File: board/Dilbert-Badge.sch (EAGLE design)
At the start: 28 parts, among them IC1 MCP23017SO, J5 I2C, J6 UART, J7 NEOPIXEL, SW1 UP, SW2 DOWN, SW3 LEFT, SW4 RIGHT, SW5 A, SW6 B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

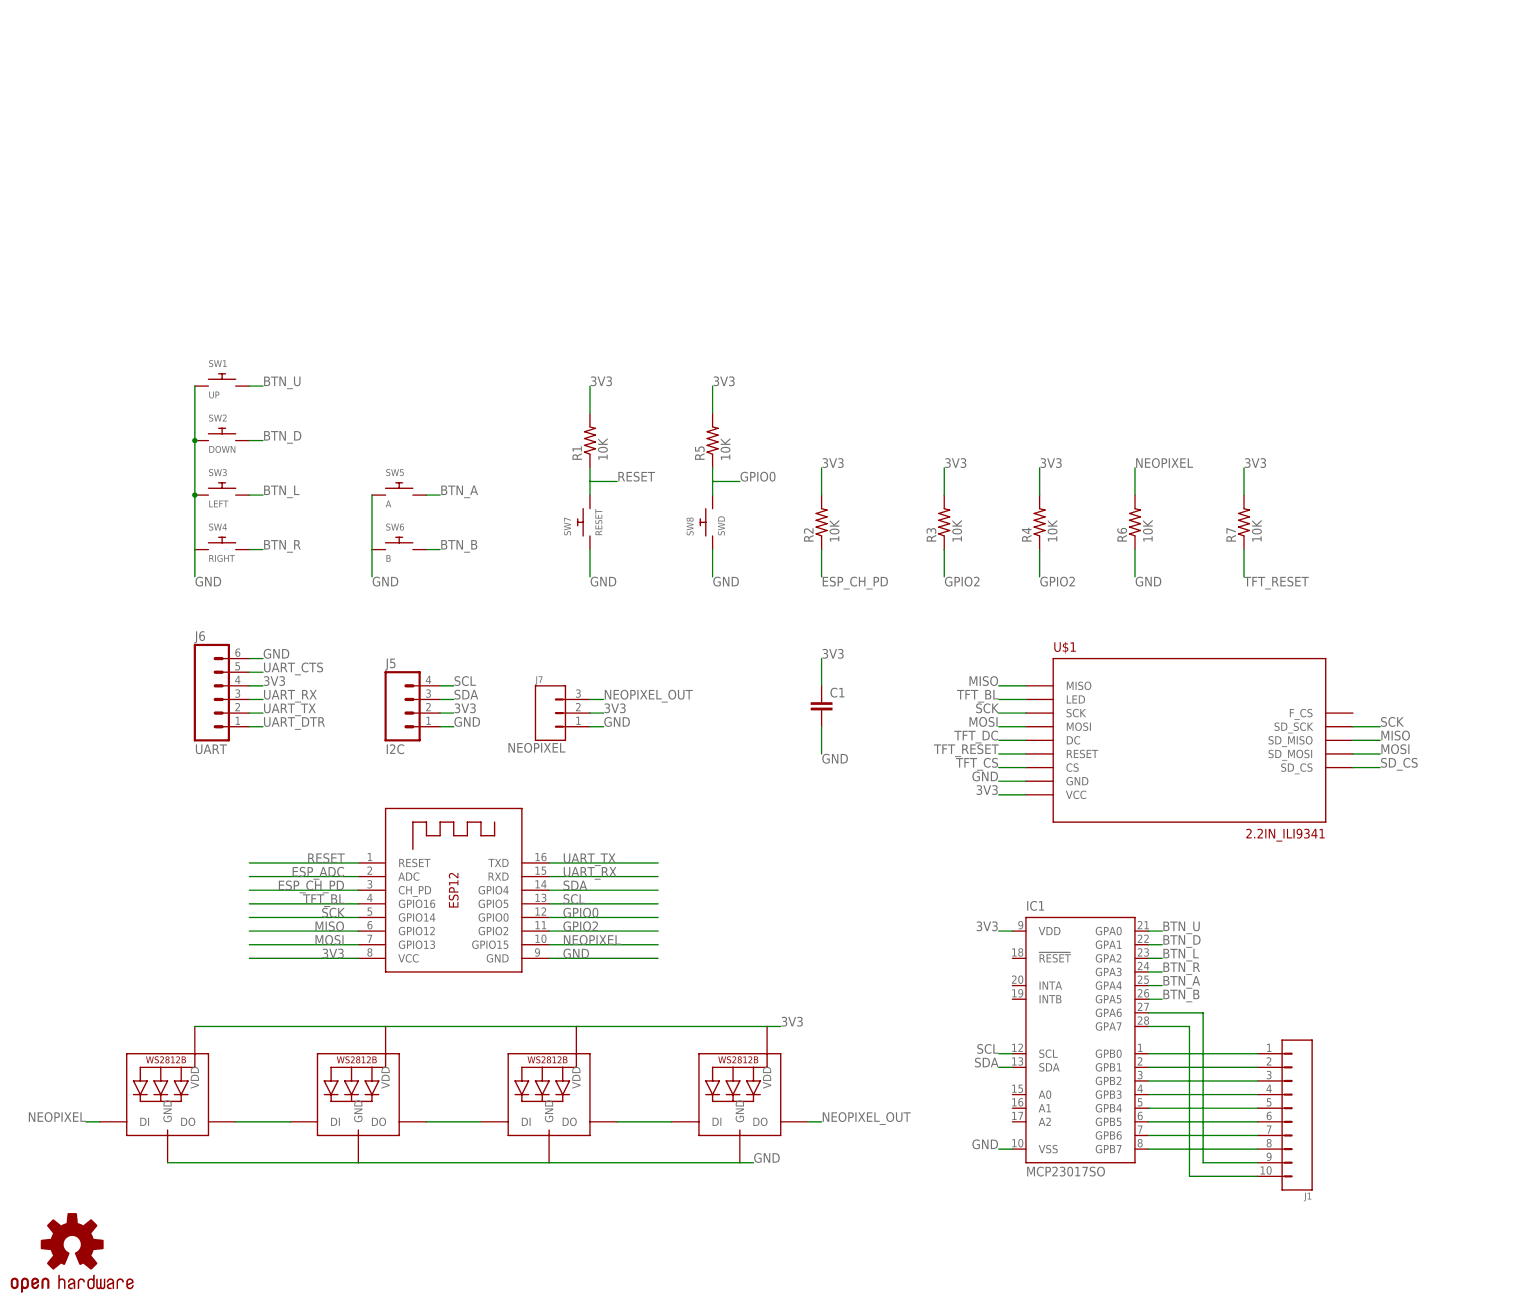
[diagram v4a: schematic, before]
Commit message: more neopixels are good
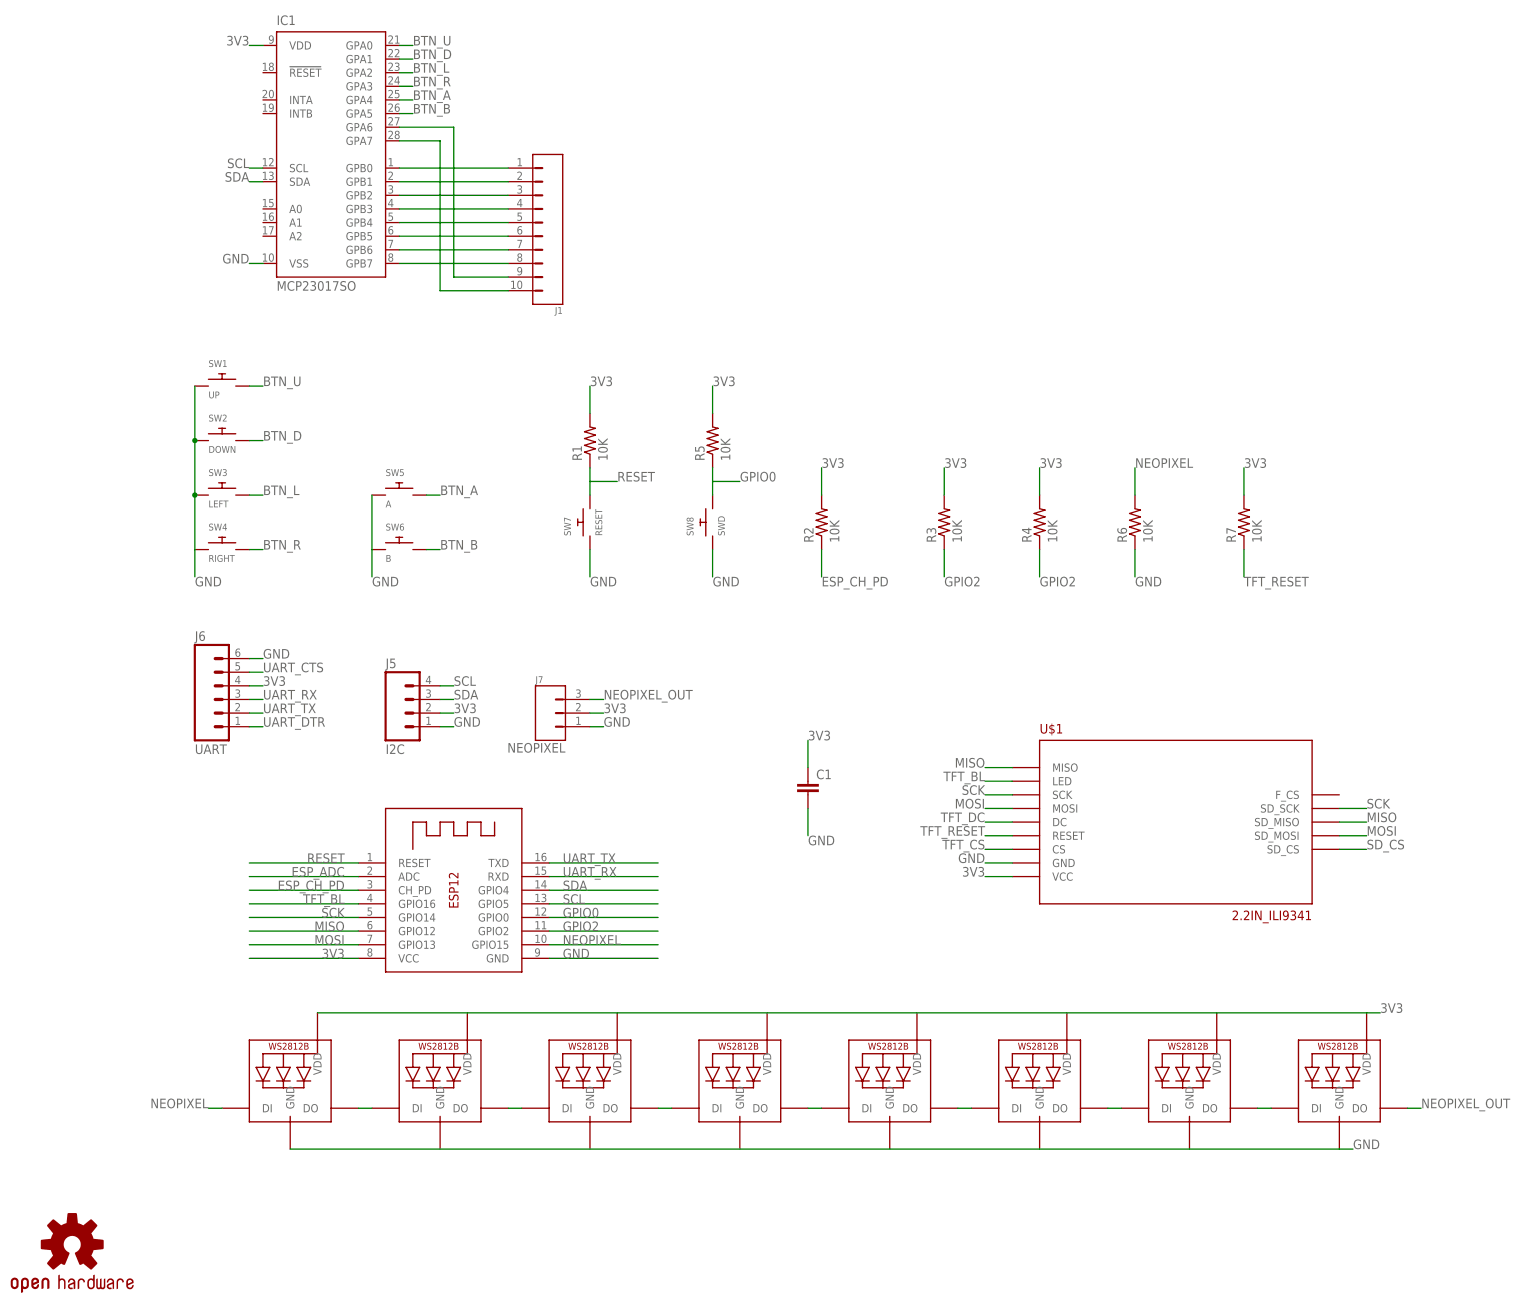
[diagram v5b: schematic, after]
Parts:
- added LED5, LED6, LED7, LED8: WS2812B5050, adafruit:WS2812B5050
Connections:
- new net N$16: LED4.DO, LED5.DI
- new net N$17: LED5.DO, LED6.DI
- new net N$18: LED6.DO, LED7.DI
- new net N$19: LED7.DO, LED8.DI
- net 3V3: now also LED8.VDD; no longer LED2.VDD, LED3.VDD, LED4.VDD
- net GND: now also LED8.GND; no longer LED2.GND, LED3.GND, LED4.GND
- net NEOPIXEL_OUT: now also LED8.DO; no longer LED4.DO
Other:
- moved on the sheet: C1, IC1, J1, U$1

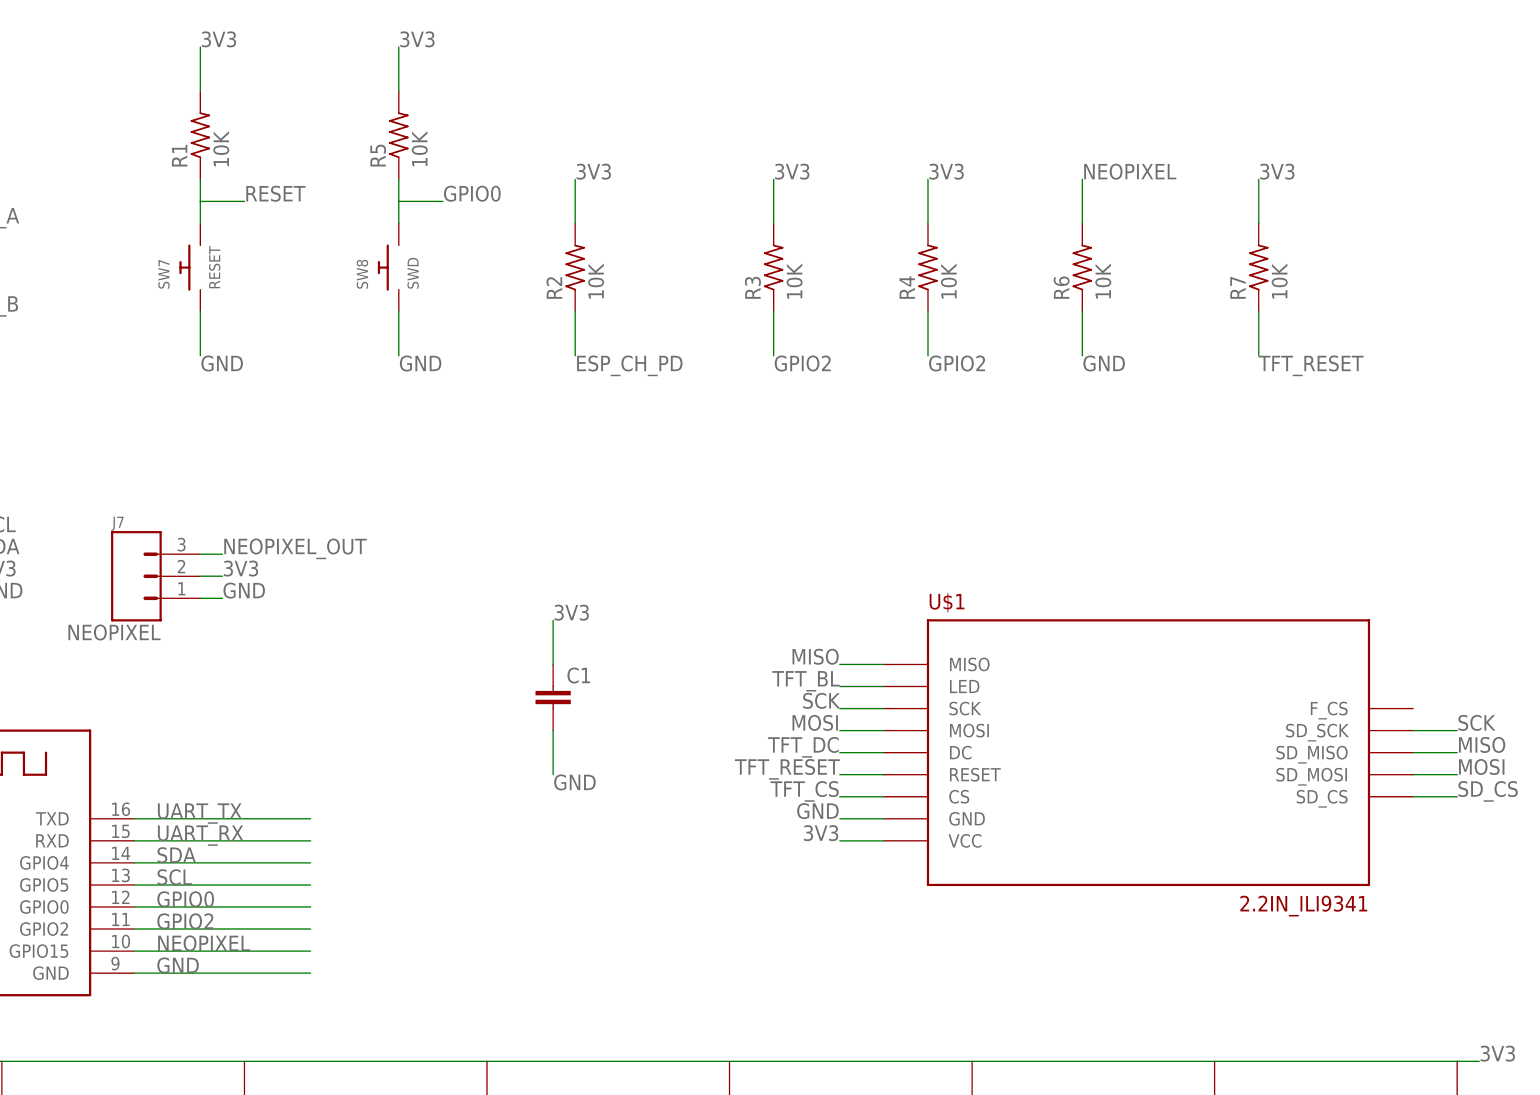
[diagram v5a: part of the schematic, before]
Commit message: switch to hardware SPI with i2c port expander
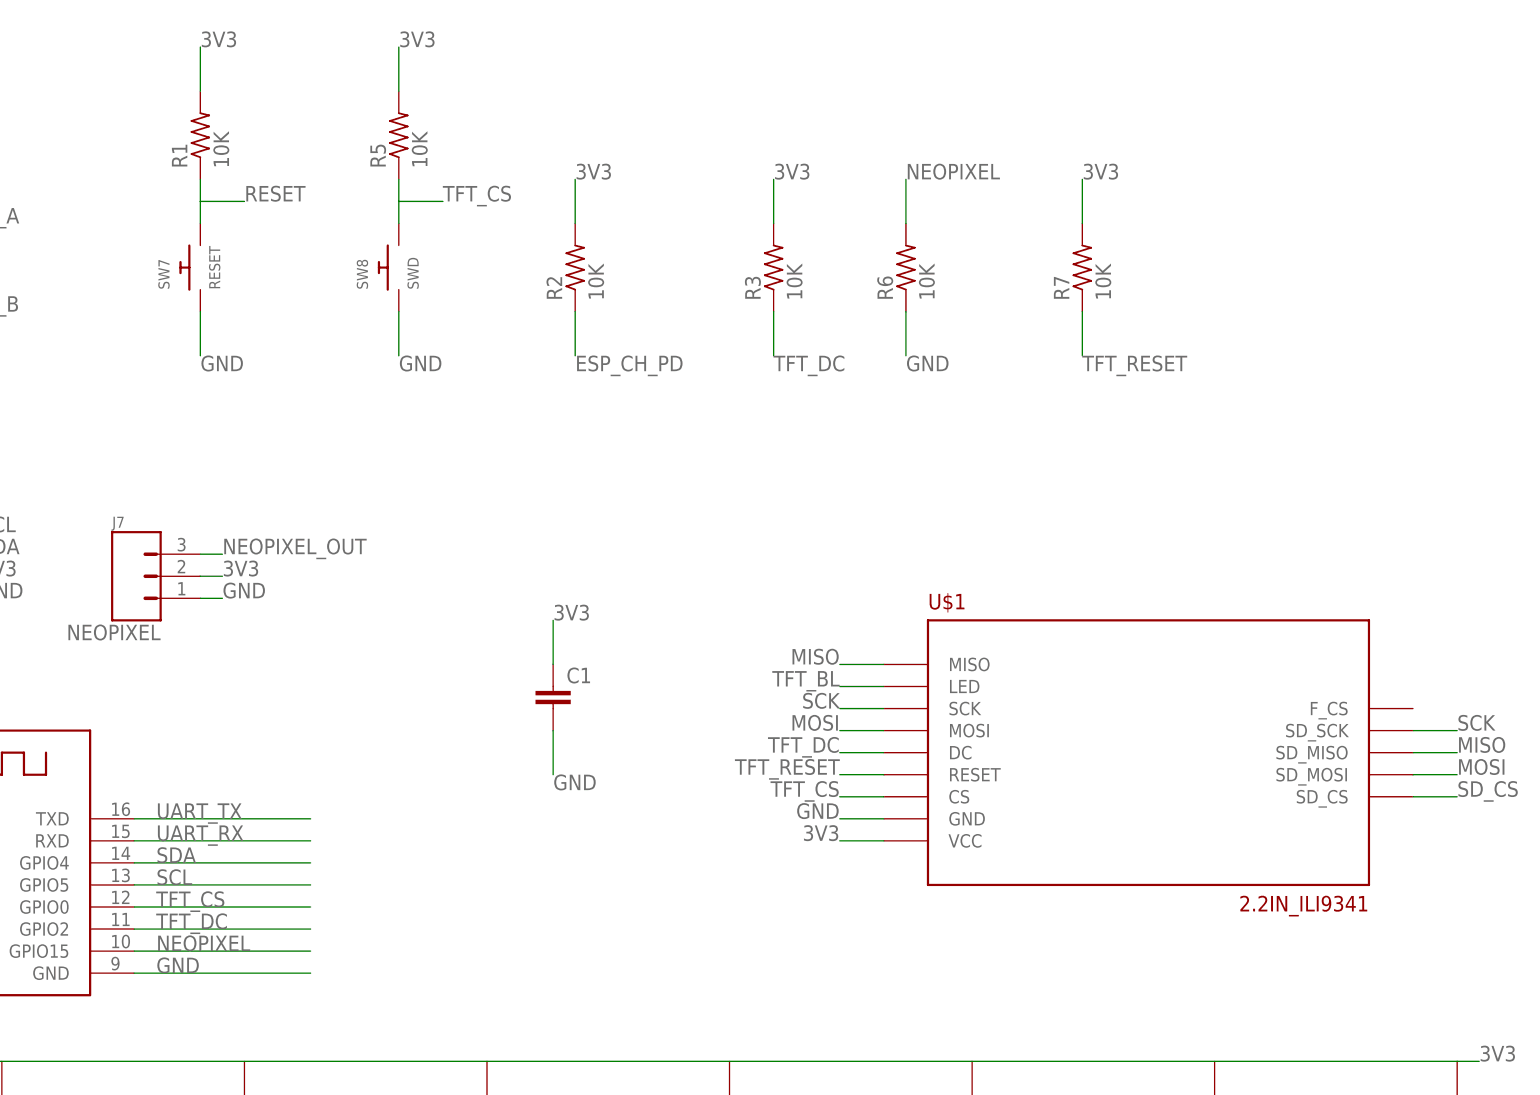
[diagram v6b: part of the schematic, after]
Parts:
- removed R4: 10K, adafruit:R-US_R0805
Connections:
- removed net GPIO0: R5.1, SW8.P$2, X1.GPIO0
- removed net GPIO2: R3.1, R4.1, X1.GPIO2
- net 3V3: no longer R4.2
- net TFT_CS: now also R5.1, SW8.P$2, X1.GPIO0
- net TFT_DC: now also R3.1, X1.GPIO2
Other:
- moved on the sheet: R6, R7
